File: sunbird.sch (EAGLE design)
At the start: 46 parts, among them J1 USB_MINI-B_SMT, Q8010 600mA/40V, U1000 TP4056, U1500 FS312F-G, U1550 FS8205, U2000 MT3608, U4000 FM116B, U5000 CH340G, Y5000 12Mhz

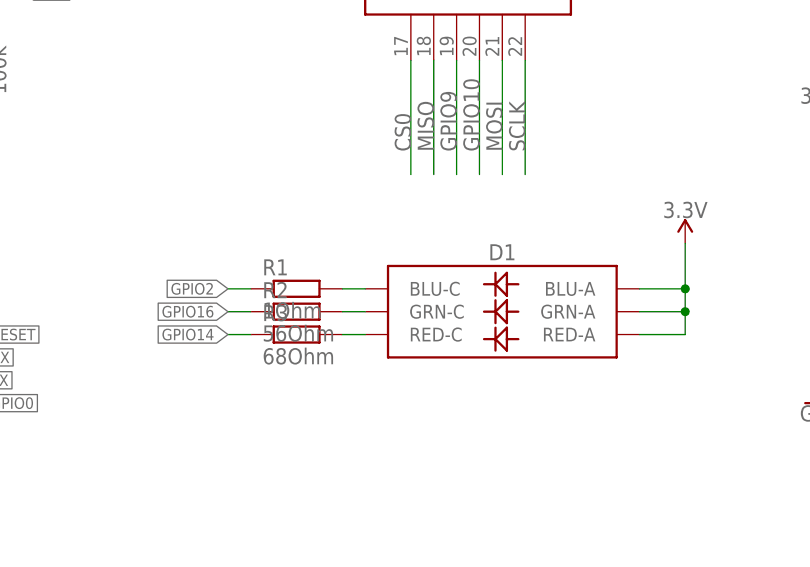
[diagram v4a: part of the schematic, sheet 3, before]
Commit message: Renumber status resistors, reposition labels
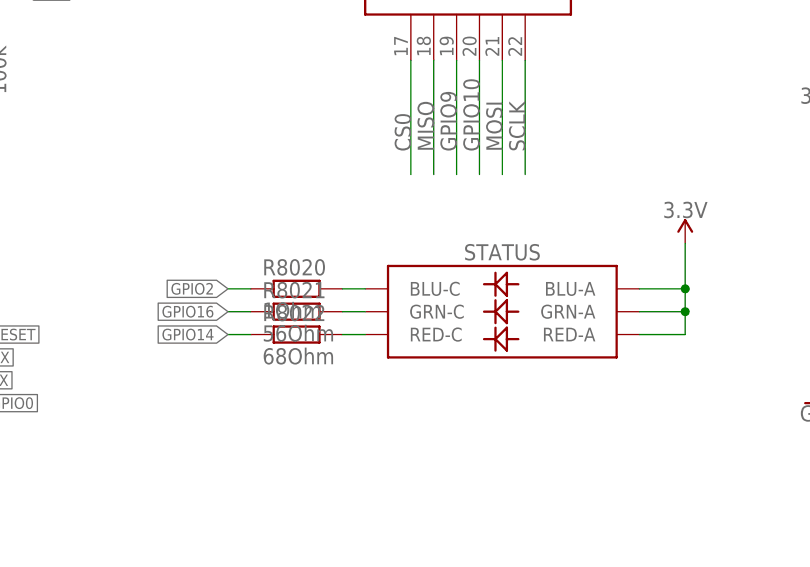
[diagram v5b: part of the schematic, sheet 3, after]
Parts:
- renumbered D1 to STATUS, R1 to R8020, R2 to R8021, R3 to R8022
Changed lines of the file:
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@@
 <part name="D2003" library="SparkFun-DiscreteSemi" library_urn="urn:adsk.eagle:library:514" deviceset="DIODE-SCHOTTKY" device="-PMEG4005EJ" package3d_urn="urn:adsk.eagle:package:38441/1" value=""/>
 <part name="U$1" library="geusebio" deviceset="ESP8266_PROGRAMMER" device=""/>
-<part name="D1" library="SparkFun-LED" library_urn="urn:adsk.eagle:library:529" deviceset="LED-RGB" device="NO_IC" package3d_urn="urn:adsk.eagle:package:39374/1"/>
+<part name="STATUS" library="SparkFun-LED" library_urn="urn:adsk.eagle:library:529" deviceset="LED-RGB" device="NO_IC" package3d_urn="urn:adsk.eagle:package:39374/1"/>
 <part name="SUPPLY20" library="SparkFun-PowerSymbols" library_urn="urn:adsk.eagle:library:530" deviceset="3.3V" device=""/>
-<part name="R1" library="rcl" library_urn="urn:adsk.eagle:library:334" deviceset="R-EU_" device="R0603" value="1Ohm"/>
-<part name="R2" library="rcl" library_urn="urn:adsk.eagle:library:334" deviceset="R-EU_" device="R0603" value="56Ohm"/>
-<part name="R3" library="rcl" library_urn="urn:adsk.eagle:library:334" deviceset="R-EU_" device="R0603" value="68Ohm"/>
+<part name="R8020" library="rcl" library_urn="urn:adsk.eagle:library:334" deviceset="R-EU_" device="R0603" value="1Ohm"/>
+<part name="R8021" library="rcl" library_urn="urn:adsk.eagle:library:334" deviceset="R-EU_" device="R0603" value="56Ohm"/>
+<part name="R8022" library="rcl" library_urn="urn:adsk.eagle:library:334" deviceset="R-EU_" device="R0603" value="68Ohm"/>
 </parts>
 <sheets>
@@
 <instance part="Q8010" gate="G$1" x="33.02" y="109.22" rot="MR0"/>
 <instance part="U$1" gate="G$1" x="15.24" y="45.72"/>
-<instance part="D1" gate="G$1" x="88.9" y="53.34" rot="MR0"/>
+<instance part="STATUS" gate="G$1" x="88.9" y="53.34" rot="MR0"/>
 <instance part="SUPPLY20" gate="G$1" x="109.22" y="60.96"/>
-<instance part="R1" gate="G$1" x="66.04" y="55.88"/>
-<instance part="R2" gate="G$1" x="66.04" y="53.34"/>
-<instance part="R3" gate="G$1" x="66.04" y="50.8"/>
+<instance part="R8020" gate="G$1" x="66.04" y="55.88"/>
+<instance part="R8021" gate="G$1" x="66.04" y="53.34"/>
+<instance part="R8022" gate="G$1" x="66.04" y="50.8"/>
 </instances>
 <busses>
@@
 </segment>
 <segment>
-<pinref part="R2" gate="G$1" pin="1"/>
+<pinref part="R8021" gate="G$1" pin="1"/>
 <wire x1="58.42" y1="53.34" x2="60.96" y2="53.34" width="0.1524" layer="91"/>
 <label x="58.42" y="53.34" size="1.27" layer="95" rot="R180" xref="yes"/>
@@
 </segment>
 <segment>
-<pinref part="D1" gate="G$1" pin="BLU-A"/>
+<pinref part="STATUS" gate="G$1" pin="BLU-A"/>
 <wire x1="104.14" y1="55.88" x2="109.22" y2="55.88" width="0.1524" layer="91"/>
 <pinref part="SUPPLY20" gate="G$1" pin="3.3V"/>
 <wire x1="109.22" y1="55.88" x2="109.22" y2="60.96" width="0.1524" layer="91"/>
-<pinref part="D1" gate="G$1" pin="GRN-A"/>
+<pinref part="STATUS" gate="G$1" pin="GRN-A"/>
 <wire x1="104.14" y1="53.34" x2="109.22" y2="53.34" width="0.1524" layer="91"/>
 <wire x1="109.22" y1="53.34" x2="109.22" y2="55.88" width="0.1524" layer="91"/>
 <junction x="109.22" y="55.88"/>
-<pinref part="D1" gate="G$1" pin="RED-A"/>
+<pinref part="STATUS" gate="G$1" pin="RED-A"/>
 <wire x1="104.14" y1="50.8" x2="109.22" y2="50.8" width="0.1524" layer="91"/>
 <wire x1="109.22" y1="50.8" x2="109.22" y2="53.34" width="0.1524" layer="91"/>
@@
 </segment>
 <segment>
-<pinref part="R3" gate="G$1" pin="1"/>
+<pinref part="R8022" gate="G$1" pin="1"/>
 <wire x1="60.96" y1="50.8" x2="58.42" y2="50.8" width="0.1524" layer="91"/>
 <label x="58.42" y="50.8" size="1.27" layer="95" rot="R180" xref="yes"/>
@@
 </segment>
 <segment>
-<pinref part="R1" gate="G$1" pin="1"/>
+<pinref part="R8020" gate="G$1" pin="1"/>
 <wire x1="60.96" y1="55.88" x2="58.42" y2="55.88" width="0.1524" layer="91"/>
 <label x="58.42" y="55.88" size="1.27" layer="95" rot="R180" xref="yes"/>
@@
 <net name="N$14" class="0">
 <segment>
-<pinref part="R1" gate="G$1" pin="2"/>
-<pinref part="D1" gate="G$1" pin="BLU-C"/>
+<pinref part="R8020" gate="G$1" pin="2"/>
+<pinref part="STATUS" gate="G$1" pin="BLU-C"/>
 <wire x1="71.12" y1="55.88" x2="73.66" y2="55.88" width="0.1524" layer="91"/>
 </segment>
@@
 <net name="N$15" class="0">
 <segment>
-<pinref part="D1" gate="G$1" pin="GRN-C"/>
-<pinref part="R2" gate="G$1" pin="2"/>
+<pinref part="STATUS" gate="G$1" pin="GRN-C"/>
+<pinref part="R8021" gate="G$1" pin="2"/>
 <wire x1="73.66" y1="53.34" x2="71.12" y2="53.34" width="0.1524" layer="91"/>
 </segment>
@@
 <net name="N$16" class="0">
 <segment>
-<pinref part="R3" gate="G$1" pin="2"/>
-<pinref part="D1" gate="G$1" pin="RED-C"/>
+<pinref part="R8022" gate="G$1" pin="2"/>
+<pinref part="STATUS" gate="G$1" pin="RED-C"/>
 <wire x1="71.12" y1="50.8" x2="73.66" y2="50.8" width="0.1524" layer="91"/>
 </segment>

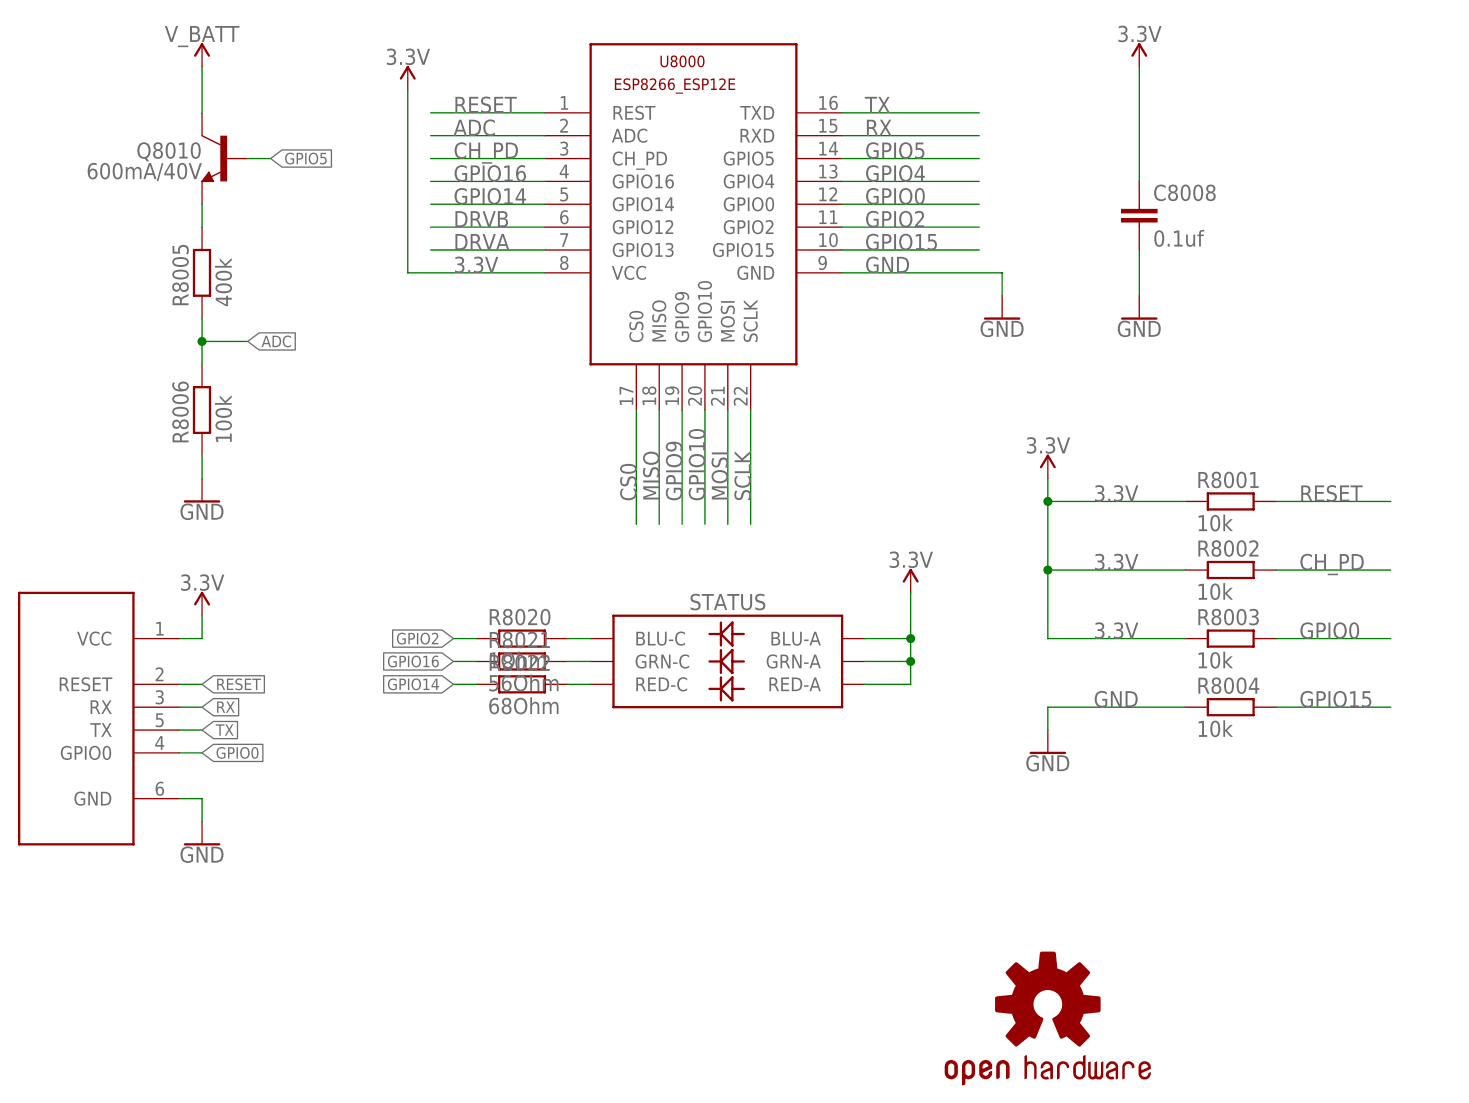
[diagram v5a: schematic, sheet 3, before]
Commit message: Change LED signal names for clarity.
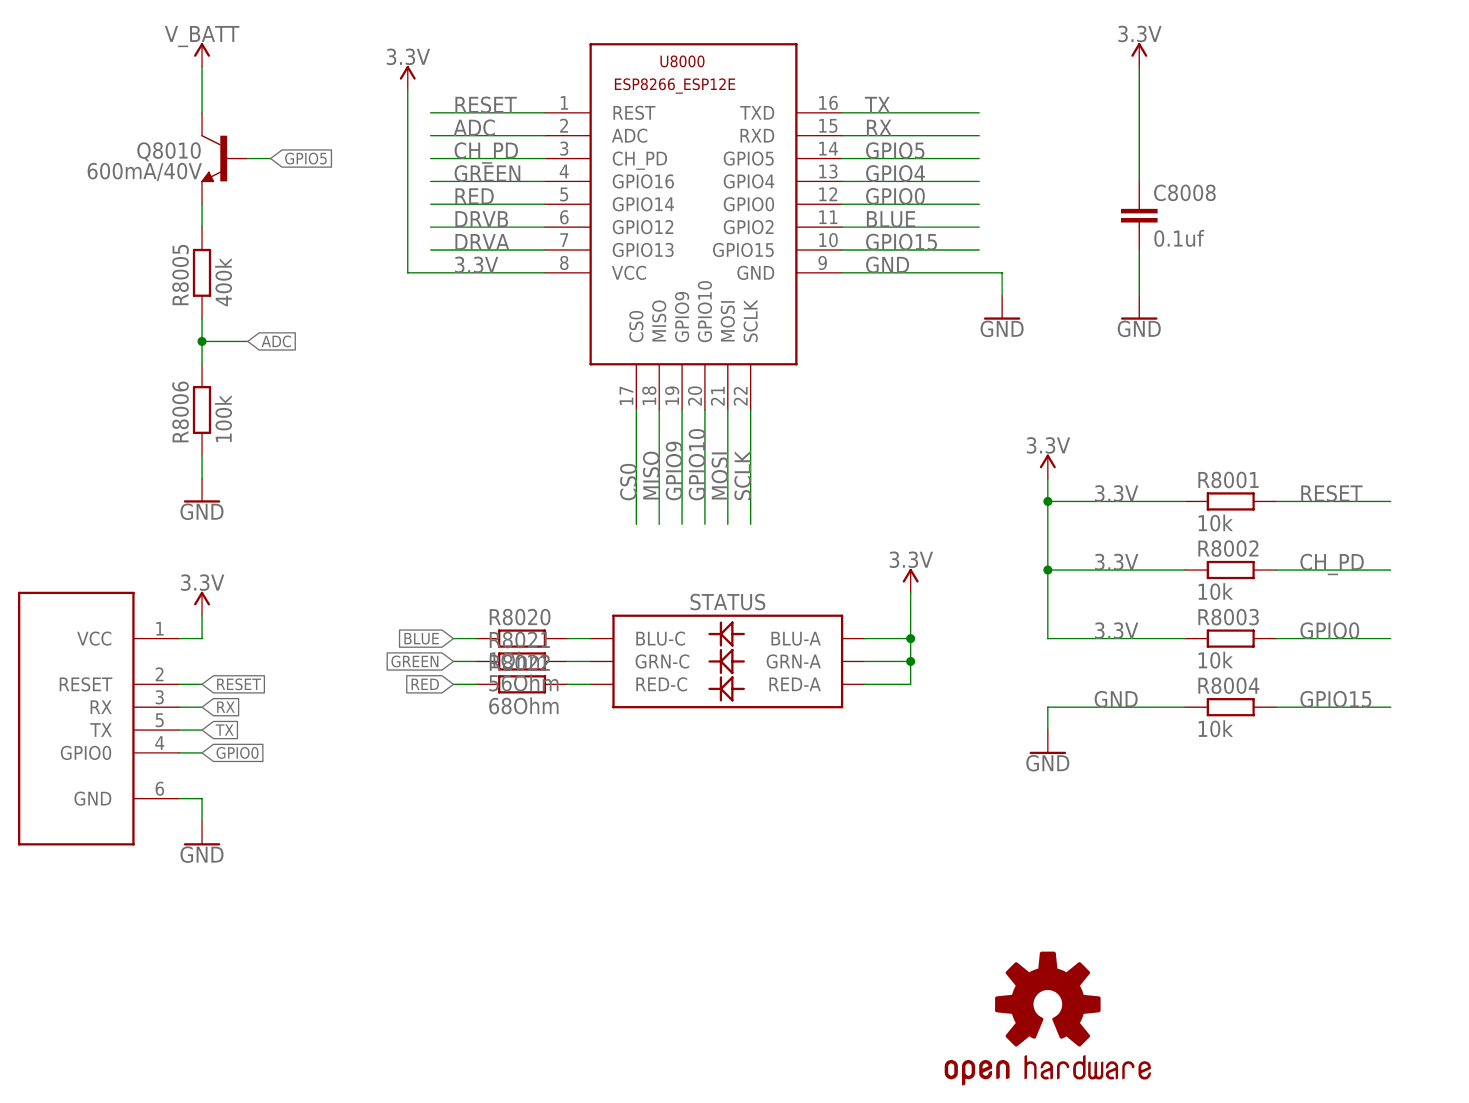
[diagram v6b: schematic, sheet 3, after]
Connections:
- net GPIO14 renamed RED
- net GPIO16 renamed GREEN
- net GPIO2 renamed BLUE
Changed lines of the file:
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@@
 </segment>
 </net>
-<net name="GPIO16" class="0">
+<net name="GREEN" class="0">
 <segment>
 <pinref part="U8000" gate="G$1" pin="GPIO16"/>
@@
 </segment>
 </net>
-<net name="GPIO14" class="0">
+<net name="RED" class="0">
 <segment>
 <pinref part="U8000" gate="G$1" pin="GPIO14"/>
@@
 </segment>
 </net>
-<net name="GPIO2" class="0">
+<net name="BLUE" class="0">
 <segment>
 <pinref part="U8000" gate="G$1" pin="GPIO2"/>

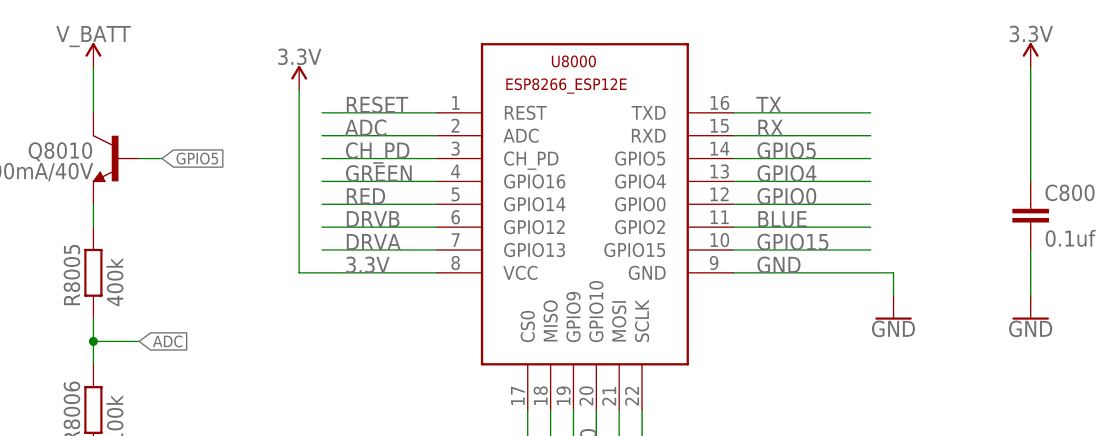
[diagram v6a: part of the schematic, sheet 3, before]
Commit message: Rename GPIO5 to BATT_SAMP_EN
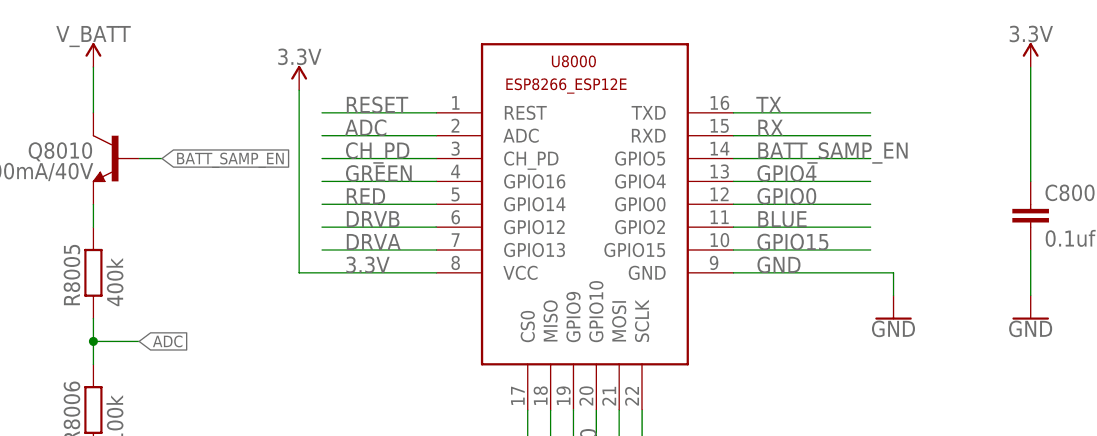
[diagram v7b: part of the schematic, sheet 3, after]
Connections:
- net GPIO5 renamed BATT_SAMP_EN
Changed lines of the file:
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@@
 </segment>
 </net>
-<net name="GPIO5" class="0">
+<net name="BATT_SAMP_EN" class="0">
 <segment>
 <pinref part="U8000" gate="G$1" pin="GPIO5"/>

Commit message: Revise the mess I made of the power regulators, add accellerometer. Motor now has a beefier 5v rail.
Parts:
- removed D2003: DIODE-SCHOTTKY-PMEG4005EJ, SparkFun-DiscreteSemi:DIODE-SCHOTTKY-PMEG4005EJ
- added 3V3, ADC, CHPD, DRVA, DRVB, GND, GP0, RST, RX, TX: TPSTP10R, testpad:TPSTP10R
- added C2104: 47uF, rcl:CPOL-EUUD-5X5,8
- added L2101: 4.7uH, SparkFun-Coils:INDUCTOR-0805-3.3UH
- added R1, R2103, R3: 1k, rcl:R-EU_R0603
- added R2, R4: 2k, rcl:R-EU_R0603
- added R2102: 4.5k, rcl:R-EU_R0603
- added R8007: 100k, rcl:R-EU_R0603
- added U2100: M3406, geusebio:M3406
- added U6000: RICHTEK-RT3000CGQM, geusebio:RICHTEK-RT3000CGQM
- added U6001: 0.1uF, rcl:C-EUC0603
- L2001: value 22uH -> 10uH; device SparkFun-Coils:INDUCTOR-SRN6045-33UH -> SparkFun-Coils:INDUCTOR-0805-3.3UH
- R1001: value 2k -> 1.2k
- R1501: value 2k -> 1k
- R2004: value 4.5k -> 7.5k
- R8005: value 400k -> 10k
- R8006: value 100k -> 400k
- R8020: value 1Ohm -> 56Ohm
- R8021: value 56Ohm -> 1Ohm
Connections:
- net N$1 renamed OC
- net N$10 renamed FS_V_BATT
- net N$11 renamed FS_CS
- net N$17 renamed V_USB_UNFUSED
- net N$8 renamed OD
- removed net GPIO10: U8000.GPIO10
- removed net GPIO9: U8000.GPIO9
- removed net N$12: D2002.A, D2003.A, L2001.2, U2000.SW
- removed net N$3: R1003.1, U1000.STDBY
- removed net N$5: BT1.-, C1503.2, U1500.GND, U1550.S2
- new net 5V: C2006.+, C4001.1, D2002.C, R2004.2, U4000.VDD
- new net BUCK: D2002.A, L2001.2, U2000.SW
- new net CHRG: R1.2, R1002.1, U1000.CHRG
- new net CHRG_3V3: R1.1, R2.2, U8000.GPIO9
- new net GND_BATT: BT1.-, C1503.2, R1501.1, U1500.GND, U1550.S2
- new net N$1: L2101.1, U2100.SW
- new net STDBY: R1003.1, R3.2, U1000.STDBY
- new net STDBY_3V3: R3.1, R4.2, U8000.GPIO10
- net 3.3V: now also 3V3.PP, C2104.+, L2101.2, R2102.2, R8004.1, U6000.VDD, U6000.VDDIO, U6001.1; no longer C2006.+, C4001.1, D2002.C, D2003.C, R2004.2, U4000.VDD
- net ADC: now also ADC.PP, R8006.1, R8007.2; no longer R8005.1, R8006.2
- net BLUE: now also R8021.1, U8000.GPIO16; no longer R8020.1, U8000.GPIO2
- net CH_PD: now also CHPD.PP
- net DRVA: now also DRVA.PP
- net DRVB: now also DRVB.PP
- net GND: now also C2104.-, GND.PP, R2.1, R2103.1, R4.1, R8005.1, R8007.1, U2100.GND, U6000.GND, U6001.2; no longer R1501.1, R8004.1, R8006.1
- net GPIO0: now also GP0.PP, U6000.SCL
- net GPIO15: now also R8005.2, U6000.INT1; no longer R8004.2
- net GPIO4: now also R8004.2, U6000.SDA
- net GREEN: now also R8020.1, U8000.GPIO2; no longer R8021.1, U8000.GPIO16
- net N$2: now also R2102.1, R2103.2, U2100.FB; no longer R1002.1, U1000.CHRG
- net N$9: now also R8006.2; no longer R8005.2
- net RESET: now also RST.PP
- net RX: now also RX.PP
- net TX: now also TX.PP
- net V_BATT: now also U2100.RUN, U2100.VIN
